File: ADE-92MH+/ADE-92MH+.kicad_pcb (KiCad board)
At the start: 2 copper layers, 60 x 30 mm, 129 parts, among them U1 ADE-92MH+, X1 SMA-F, X2 SMA-F, X3 SMA-F

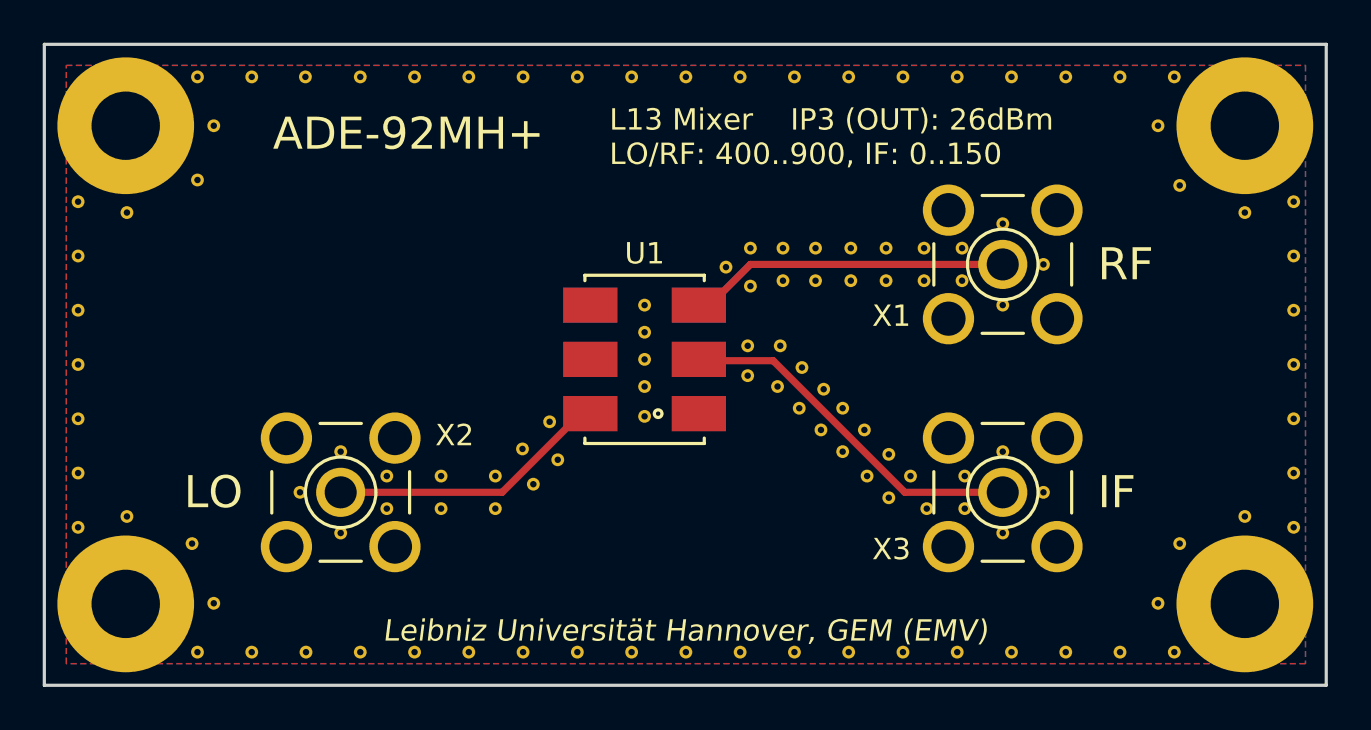
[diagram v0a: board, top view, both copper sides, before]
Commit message: ADE-92MH+: corrected 50Ohm CPW, new VIA arrangement
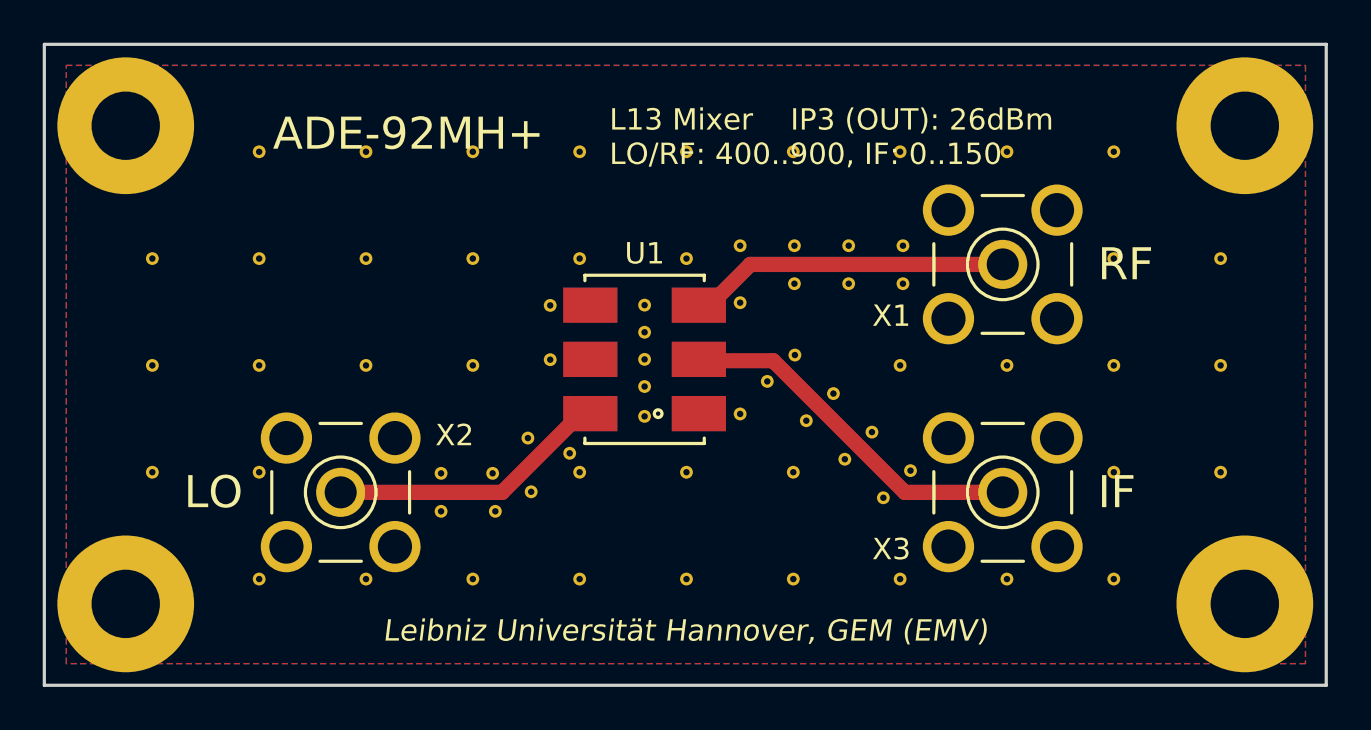
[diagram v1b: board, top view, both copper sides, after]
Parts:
- removed REF**211 (x2), REF**2111 (x8), REF**2112 (x2), REF**2113 (x2), REF**2114 (x2), REF**2115 (x2), REF**2116 (x2), REF**2117 (x8), REF**221 (x2), REF**23111 (x4), REF**241 (x2), REF**251 (x2), REF**261 (x2), REF**2711 (x2), REF**2721 (x2), REF**2731 (x2), REF**2741 (x2), REF**2751 (x2), REF**2761 (x2), REF**27711 (x2), REF**27721 (x2), REF**27731 (x2), REF**27741 (x2), REF**27751 (x2), REF**27761 (x2), REF**27771 (x2): VIA-0.3, JueVias:VIA-0.3
- removed the REF**231 at (121.9, 100.4)
- removed the REF**231 at (127.7, 101.1)
- removed the REF**231 at (129.4, 101.1)
- removed the REF**231 at (122.9, 104.1)
- removed the REF**231 at (124.4, 104.1)
- removed the REF**231 at (125.5, 105.1)
- removed the REF**231 at (126.5, 106.1)
- removed the REF**231 at (127.4, 107.0)
- removed the REF**231 at (128.4, 108.0)
- removed the REF**231 at (129.5, 109.2)
- removed the REF**231 at (122.9, 105.5)
- removed the REF**231 at (123.0, 99.5)
- removed the REF**231 at (124.3, 106.0)
- removed the REF**231 at (125.3, 107.0)
- removed the REF**231 at (126.3, 108.0)
- removed the REF**231 at (127.4, 109.1)
- removed the REF**231 at (128.5, 110.2)
- removed the REF**231 at (129.5, 111.2)
- removed the REF**231 at (124.6, 99.5)
- removed the REF**231 at (114.0, 109.4)
- removed the REF**231 at (112.9, 110.6)
- removed the REF**231 at (113.7, 107.7)
- removed the REF**231 at (112.4, 108.9)
- removed the REF**231 at (111.1, 111.7)
- removed the REF**231 at (134.9, 112.9)
- removed the REF**231 at (136.8, 111.0)
- removed the REF**231 at (134.9, 109.1)
- removed the REF**231 at (136.8, 100.3)
- removed the REF**231 at (126.1, 99.5)
- removed the REF**231 at (134.9, 102.2)
- removed the REF**231 at (134.9, 98.4)
- removed the REF**231 at (133.0, 99.5)
- removed the REF**231 at (131.2, 99.5)
- removed the REF**231 at (133.0, 101.1)
- removed the REF**231 at (131.2, 101.1)
- removed the REF**231 at (103.9, 112.9)
- removed the REF**231 at (102.0, 111.0)
- removed the REF**231 at (103.9, 109.1)
- removed the REF**231 at (111.1, 110.2)
- removed the REF**231 at (127.7, 99.5)
- removed the REF**231 at (108.6, 110.2)
- removed the REF**231 at (106.0, 110.2)
- removed the REF**231 at (106.0, 111.7)
- removed the REF**231 at (108.6, 111.7)
- removed the REF**231 at (102.2, 118.4)
- removed the REF**231 at (102.2, 91.5)
- removed the REF**231 at (129.4, 99.5)
- removed the REF**231 at (123.0, 101.3)
- removed the REF**231 at (124.6, 101.1)
- removed the REF**231 at (126.1, 101.1)
- added REF**231: VIA-0.3, JueVias:VIA-0.3, F.Cu at (123.8, 105.8)
- added REF**231: VIA-0.3, JueVias:VIA-0.3, F.Cu at (125.1, 99.4)
- added REF**231: VIA-0.3, JueVias:VIA-0.3, F.Cu at (127.6, 99.4)
- added REF**231: VIA-0.3, JueVias:VIA-0.3, F.Cu at (130.2, 99.4)
- added REF**231: VIA-0.3, JueVias:VIA-0.3, F.Cu at (125.7, 107.6)
- added REF**231: VIA-0.3, JueVias:VIA-0.3, F.Cu at (127.5, 109.4)
- added REF**231: VIA-0.3, JueVias:VIA-0.3, F.Cu at (129.3, 111.2)
- added REF**231: VIA-0.3, JueVias:VIA-0.3, F.Cu at (125.1, 104.5)
- added REF**231: VIA-0.3, JueVias:VIA-0.3, F.Cu at (126.9, 106.3)
- added REF**231: VIA-0.3, JueVias:VIA-0.3, F.Cu at (128.7, 108.1)
- added REF**231: VIA-0.3, JueVias:VIA-0.3, F.Cu at (130.5, 110.0)
- added REF**231: VIA-0.3, JueVias:VIA-0.3, F.Cu at (122.6, 107.3)
- added REF**231: VIA-0.3, JueVias:VIA-0.3, F.Cu at (112.6, 108.4)
- added REF**231: VIA-0.3, JueVias:VIA-0.3, F.Cu at (114.6, 109.1)
- added REF**231: VIA-0.3, JueVias:VIA-0.3, F.Cu at (112.8, 110.9)
- added REF**231: VIA-0.3, JueVias:VIA-0.3, F.Cu at (111.0, 110.1)
- added REF**231: VIA-0.3, JueVias:VIA-0.3, F.Cu at (111.1, 111.9)
- added REF**231: VIA-0.3, JueVias:VIA-0.3, F.Cu at (108.6, 111.9)
- added REF**231: VIA-0.3, JueVias:VIA-0.3, F.Cu at (108.6, 110.1)
- added REF**231: VIA-0.3, JueVias:VIA-0.3, F.Cu at (113.7, 102.2)
- added REF**231: VIA-0.3, JueVias:VIA-0.3, F.Cu at (113.7, 104.8)
- added REF**231: VIA-0.3, JueVias:VIA-0.3, F.Cu at (122.6, 102.1)
- added REF**231: VIA-0.3, JueVias:VIA-0.3, F.Cu at (125.1, 101.2)
- added REF**231: VIA-0.3, JueVias:VIA-0.3, F.Cu at (127.6, 101.2)
- added REF**231: VIA-0.3, JueVias:VIA-0.3, F.Cu at (130.2, 101.2)
- added REF**231: VIA-0.3, JueVias:VIA-0.3, F.Cu at (122.6, 99.4)
- added REF**23102: VIA-0.3, JueVias:VIA-0.3, F.Cu at (135.1, 95.0)
- added REF**23104: VIA-0.3, JueVias:VIA-0.3, F.Cu at (135.1, 105.0)
- added REF**23106: VIA-0.3, JueVias:VIA-0.3, F.Cu at (135.1, 115.0)
- added REF**23112: VIA-0.3, JueVias:VIA-0.3, F.Cu at (140.1, 95.0)
- added REF**23113: VIA-0.3, JueVias:VIA-0.3, F.Cu at (140.1, 100.0)
- added REF**23114: VIA-0.3, JueVias:VIA-0.3, F.Cu at (140.1, 105.0)
- added REF**23115: VIA-0.3, JueVias:VIA-0.3, F.Cu at (140.1, 110.0)
- added REF**23116: VIA-0.3, JueVias:VIA-0.3, F.Cu at (140.1, 115.0)
- added REF**23123: VIA-0.3, JueVias:VIA-0.3, F.Cu at (145.1, 100.0)
- added REF**23124: VIA-0.3, JueVias:VIA-0.3, F.Cu at (145.1, 105.0)
- added REF**23125: VIA-0.3, JueVias:VIA-0.3, F.Cu at (145.1, 110.0)
- added REF**2323: VIA-0.3, JueVias:VIA-0.3, F.Cu at (95.1, 100.0)
- added REF**2324: VIA-0.3, JueVias:VIA-0.3, F.Cu at (95.1, 105.0)
- added REF**2325: VIA-0.3, JueVias:VIA-0.3, F.Cu at (95.1, 110.0)
- added REF**2332: VIA-0.3, JueVias:VIA-0.3, F.Cu at (100.1, 95.0)
- added REF**2333: VIA-0.3, JueVias:VIA-0.3, F.Cu at (100.1, 100.0)
- added REF**2334: VIA-0.3, JueVias:VIA-0.3, F.Cu at (100.1, 105.0)
- added REF**2335: VIA-0.3, JueVias:VIA-0.3, F.Cu at (100.1, 110.0)
- added REF**2336: VIA-0.3, JueVias:VIA-0.3, F.Cu at (100.1, 115.0)
- added REF**2342: VIA-0.3, JueVias:VIA-0.3, F.Cu at (105.1, 95.0)
- added REF**2343: VIA-0.3, JueVias:VIA-0.3, F.Cu at (105.1, 100.0)
- added REF**2344: VIA-0.3, JueVias:VIA-0.3, F.Cu at (105.1, 105.0)
- added REF**2346: VIA-0.3, JueVias:VIA-0.3, F.Cu at (105.1, 115.0)
- added REF**2352: VIA-0.3, JueVias:VIA-0.3, F.Cu at (110.1, 95.0)
- added REF**2353: VIA-0.3, JueVias:VIA-0.3, F.Cu at (110.1, 100.0)
- added REF**2354: VIA-0.3, JueVias:VIA-0.3, F.Cu at (110.1, 105.0)
- added REF**2356: VIA-0.3, JueVias:VIA-0.3, F.Cu at (110.1, 115.0)
- added REF**2362: VIA-0.3, JueVias:VIA-0.3, F.Cu at (115.1, 95.0)
- added REF**2363: VIA-0.3, JueVias:VIA-0.3, F.Cu at (115.1, 100.0)
- added REF**2365: VIA-0.3, JueVias:VIA-0.3, F.Cu at (115.1, 110.0)
- added REF**2366: VIA-0.3, JueVias:VIA-0.3, F.Cu at (115.1, 115.0)
- added REF**2372: VIA-0.3, JueVias:VIA-0.3, F.Cu at (120.1, 95.0)
- added REF**2373: VIA-0.3, JueVias:VIA-0.3, F.Cu at (120.1, 100.0)
- added REF**2375: VIA-0.3, JueVias:VIA-0.3, F.Cu at (120.1, 110.0)
- added REF**2376: VIA-0.3, JueVias:VIA-0.3, F.Cu at (120.1, 115.0)
- added REF**2382: VIA-0.3, JueVias:VIA-0.3, F.Cu at (125.1, 95.0)
- added REF**2385: VIA-0.3, JueVias:VIA-0.3, F.Cu at (125.1, 110.0)
- added REF**2386: VIA-0.3, JueVias:VIA-0.3, F.Cu at (125.1, 115.0)
- added REF**2392: VIA-0.3, JueVias:VIA-0.3, F.Cu at (130.1, 95.0)
- added REF**2394: VIA-0.3, JueVias:VIA-0.3, F.Cu at (130.1, 105.0)
- added REF**2396: VIA-0.3, JueVias:VIA-0.3, F.Cu at (130.1, 115.0)
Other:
- net class 50Ohm: clearance 0.2 -> 0.15; trace_width 0.336 -> 0.714
- net class Default: clearance 0.1 -> 0.15
- rule trace_clearance: 0.1 -> 0.15
